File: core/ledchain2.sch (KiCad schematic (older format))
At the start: 40 parts

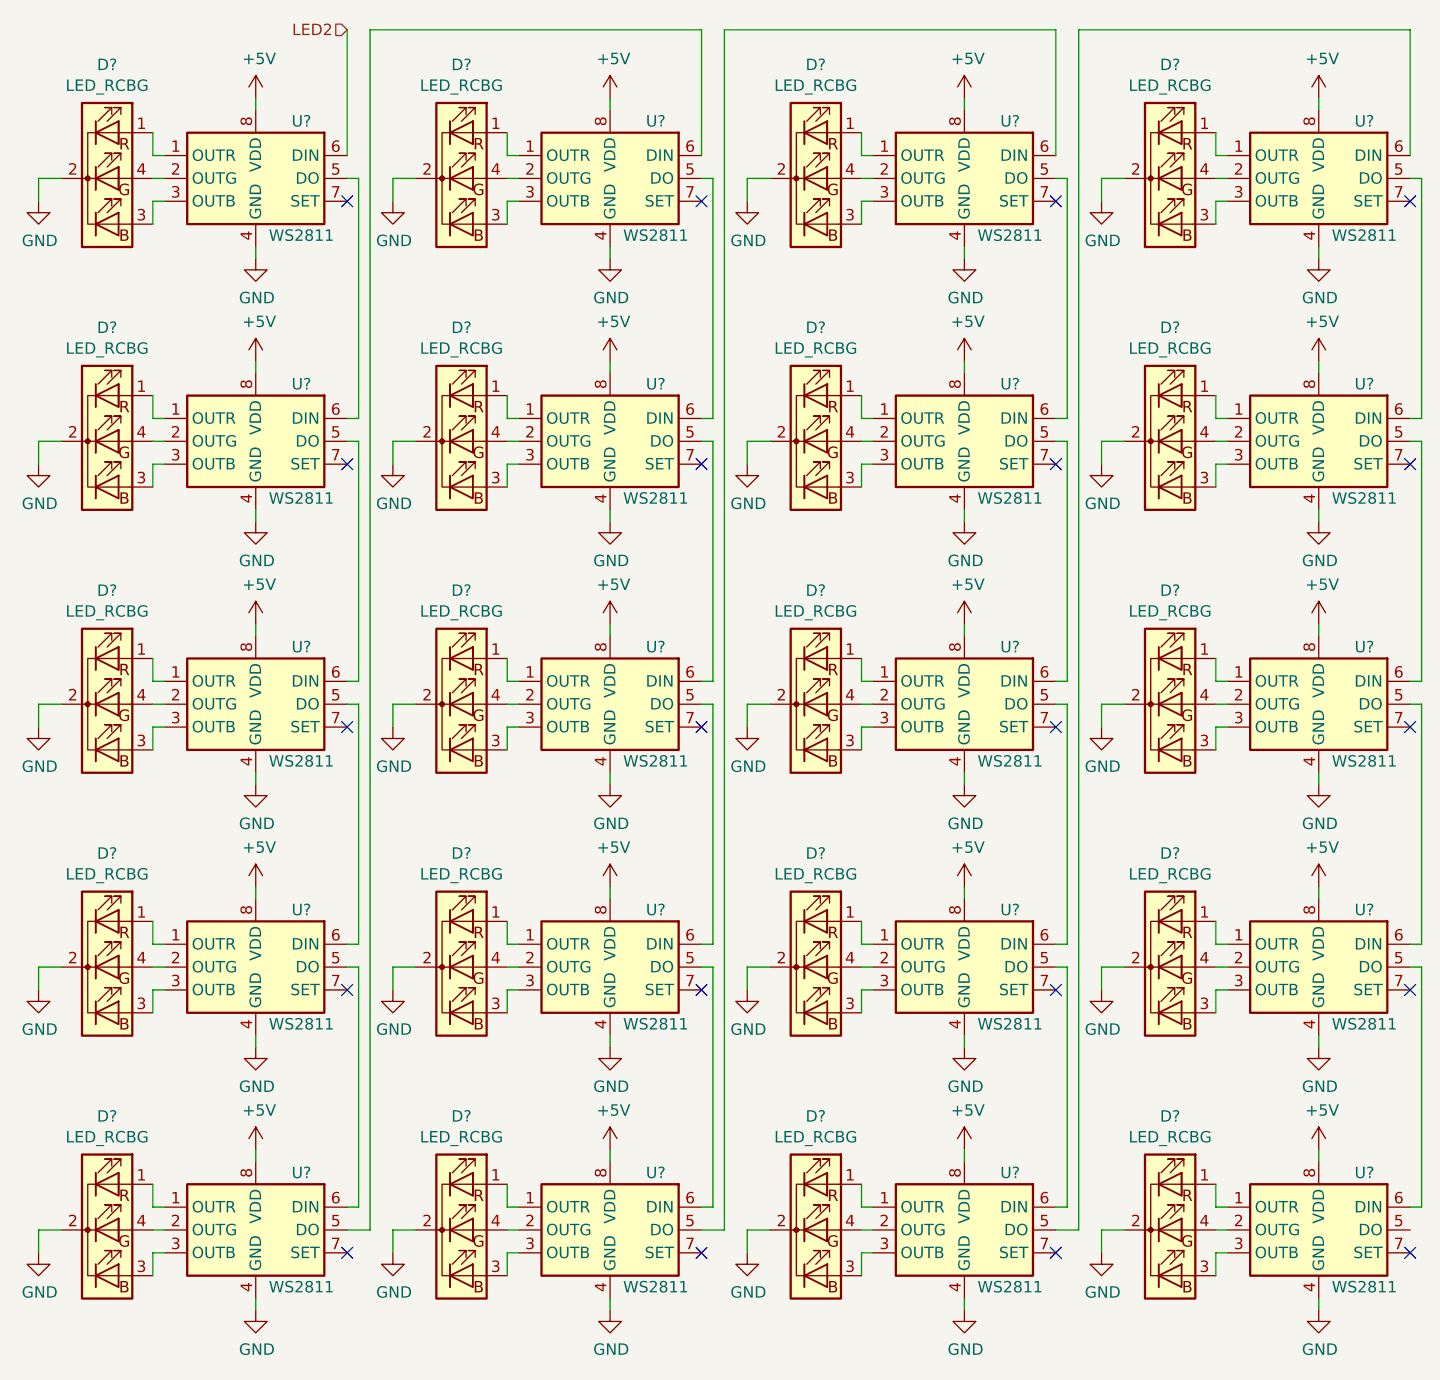
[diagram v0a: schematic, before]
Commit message: annotate led chain
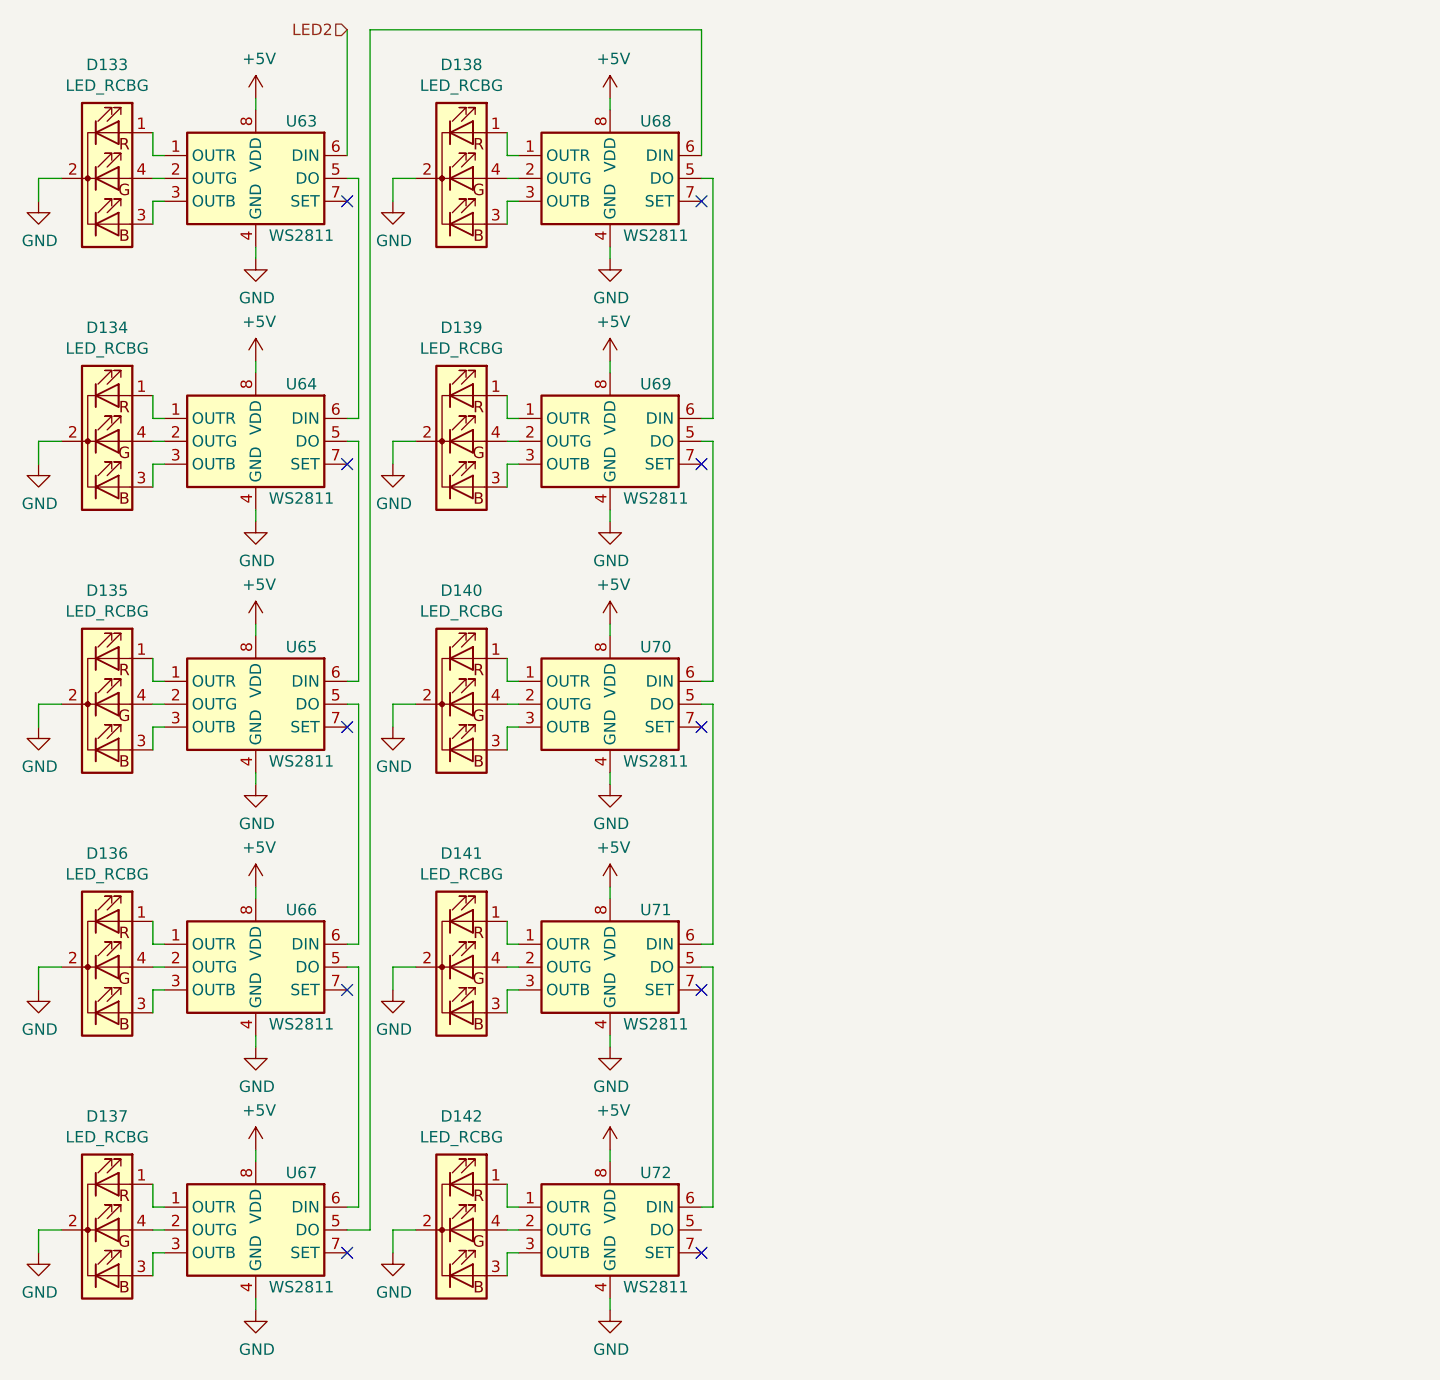
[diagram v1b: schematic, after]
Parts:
- removed D? (x10): LED_RCBG, Connector_PinHeader_1.00mm:PinHeader_1x04_P1.00mm_Horizontal, symbol Device:LED_RCBG
- removed U? (x10): WS2811, Package_SO:SOIC-8-1EP_3.9x4.9mm_P1.27mm_EP2.29x3mm, symbol Driver_LED:WS2811
- gave numbers to parts that had none: 20
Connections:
- no-connect marks 20 -> 10
